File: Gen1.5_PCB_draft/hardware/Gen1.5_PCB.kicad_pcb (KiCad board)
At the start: 4 copper layers, 93.7 x 95.8 mm, 67 parts, among them IC1 TJA1050T, J1 Enc1, J10 jumper2, J11 jumper4, J12 Enc2, J13 Enc3, J14 Enc4, J15 Enc5, J16 Enc6, J17 jumper6, J2 Booster, J4 jumper1, J5 Roboclaw1, J6 Roboclaw2, J7 Roboclaw3, J8 jumper3, J9 jumper5, P2 loadcell 1, P3 loadcell 2, P4 loadcell 3, P5 loadcell 4, U1 ESP32-P4-ETH, U2 4754, U3 INA118PB, U4 REF2033QDDCRQ1, U5 INA118PB, U6 INA118PB, U7 INA118PB, U8 level shifter

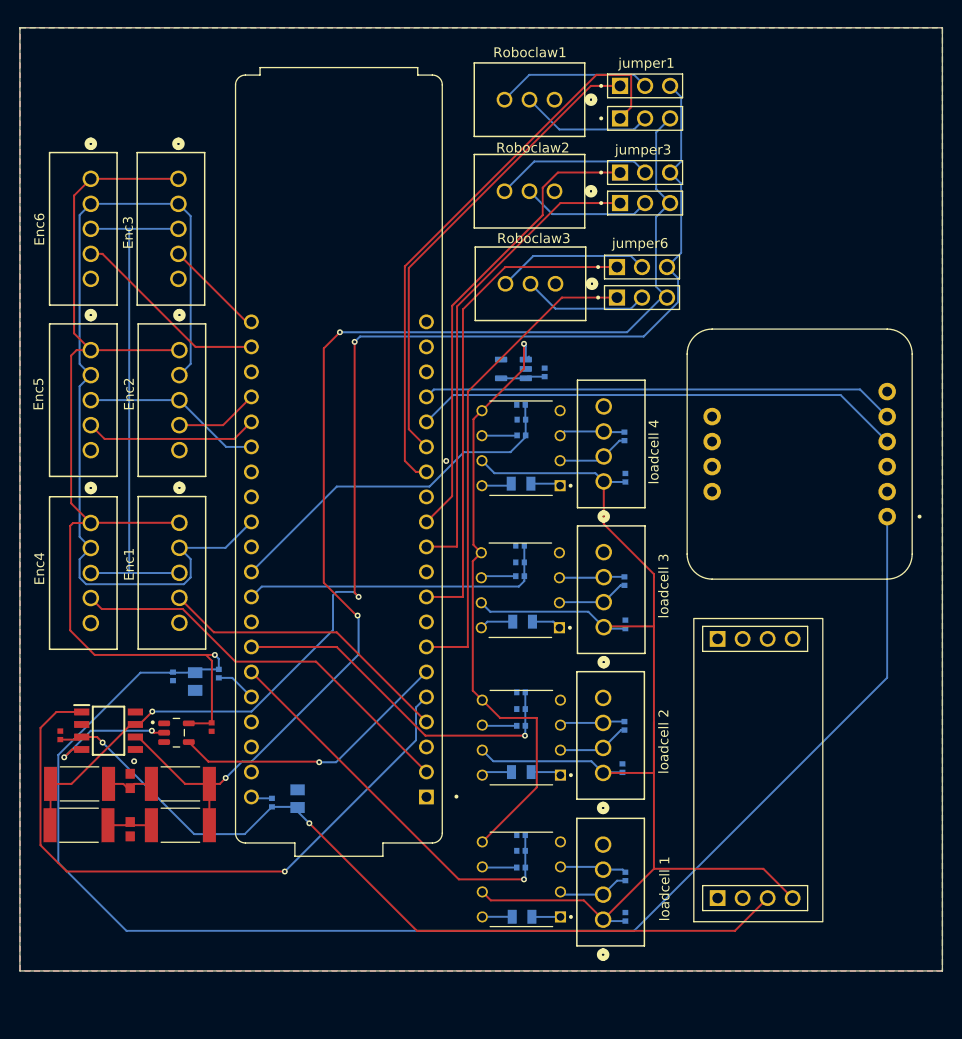
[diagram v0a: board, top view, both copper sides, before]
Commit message: added correct lcsc for decoup caps and amps and edited silkscreen labels
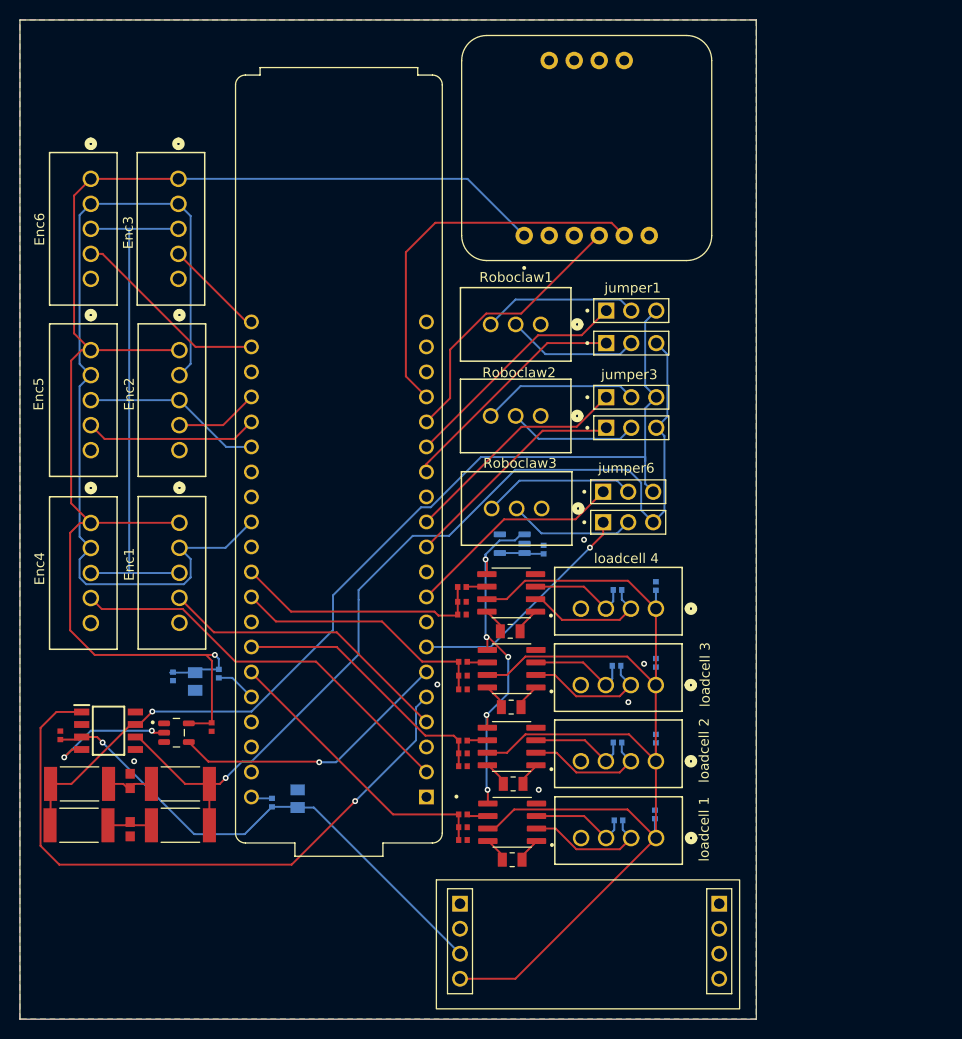
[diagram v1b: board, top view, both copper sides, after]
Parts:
- removed U3, U5, U6, U7: INA118PB, Gen1.5_PCB:INA118PB
- added U10: INA118U_2K5, Gen1.5_PCB:INA118U_2K5, F.Cu at (170.0, 102.4)
- added U11: INA118U_2K5, Gen1.5_PCB:INA118U_2K5, F.Cu at (170.0, 94.5)
- added U12: INA118U_2K5, Gen1.5_PCB:INA118U_2K5, F.Cu at (170.0, 86.8)
- added U9: INA118U_2K5, Gen1.5_PCB:INA118U_2K5, F.Cu at (170.1, 110.1)
- C11, C14, C17, C7, R10, R11, R12, R13, R14, R15, R4, R5, R6, R7, R8, R9: moved to F.Cu
- moved U2 37.9 mm to (177.7, 41.6), turned to 0 degrees
- moved J2 26.5 mm to (162.4, 116.0), turned to 0 degrees
- moved J11 22.9 mm to (182.2, 70.0)
- moved J17 22.9 mm to (181.9, 79.6)
- moved J4 22.9 mm to (182.2, 58.1)
- moved J6 22.9 mm to (173.0, 68.8)
- moved J9 22.9 mm to (181.9, 76.5)
- moved J10 22.9 mm to (182.2, 61.4)
- moved J5 22.9 mm to (173.0, 59.5)
- moved J7 22.9 mm to (173.1, 78.2)
- moved J8 22.9 mm to (182.2, 66.9)
- moved C17 22.1 mm to (165.0, 89.0), turned to 180 degrees
- moved R15 19.5 mm to (165.0, 87.7), turned to 180 degrees
- moved C8 18.0 mm to (173.3, 82.4)
- moved U4 17.8 mm to (170.1, 81.8)
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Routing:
- net /3V3: track 250.7 -> 147.5 mm
- net /TX1: track 58.3 -> 24.2 mm
- net /5V: track 84.2 -> 52.7 mm, vias 2 -> 1
- net /CANH: track 131.0 -> 101.1 mm, vias 3 -> 1
- net /RX3: track 50.3 -> 22.4 mm
- net /loadcells/Vref: track 62.7 -> 36.8 mm, vias 1 -> 5
- net /TX3: track 49.3 -> 23.9 mm, vias 0 -> 1
- net /TX2: track 48.4 -> 23.3 mm
- net /CANL: track 124.3 -> 100.1 mm, vias 3 -> 1
- net /RX1: track 48.0 -> 24.0 mm
- net /RX2: track 47.3 -> 23.5 mm
- net /SCL: track 49.9 -> 28.3 mm
- net LC1: track 41.0 -> 29.7 mm, vias 1 -> 0
- net LC4: track 36.8 -> 25.8 mm
- net 10V: track 142.7 -> 133.1 mm
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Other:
- board size 93.7 x 95.8 mm -> 74.8 x 101.5 mm
